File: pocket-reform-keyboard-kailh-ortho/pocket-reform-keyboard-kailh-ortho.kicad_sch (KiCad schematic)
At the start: 128 parts, among them SW1 Choc, SW10 Choc, SW11 Choc, SW12 Choc, SW13 Choc, SW14 Choc, SW15 Choc, SW16 Choc, SW17 Choc, SW18 Choc, SW19 Choc, SW2 Choc, SW20 Choc, SW21 Choc, SW22 Choc, SW23 Choc, SW24 Choc, SW25 Choc, SW26 Choc, SW27 Choc, SW28 Choc, SW29 Choc, SW3 Choc, SW30 Choc, SW31 Choc, SW32 Choc, SW33 Choc, SW34 Choc, SW35 Choc, SW36 Choc, SW37 Choc, SW38 Choc, SW39 Choc, SW4 Choc, SW40 Choc, SW41 Choc, SW42 Choc, SW43 Choc, SW44 Choc, SW45 Choc, SW46 Choc, SW47 Choc, SW48 Choc, SW49 Choc, SW5 Choc, SW50 Choc, SW51 Choc, SW52 Choc, SW53 Choc, SW54 Choc, SW55 Choc, SW56 Choc, SW57 Choc, SW58 Choc, SW59 Choc, SW6 Choc, SW60 Choc, SW61 Choc, SW62 Choc, SW63 Choc, SW64 Choc, SW7 Choc, SW8 Choc, SW9 Choc

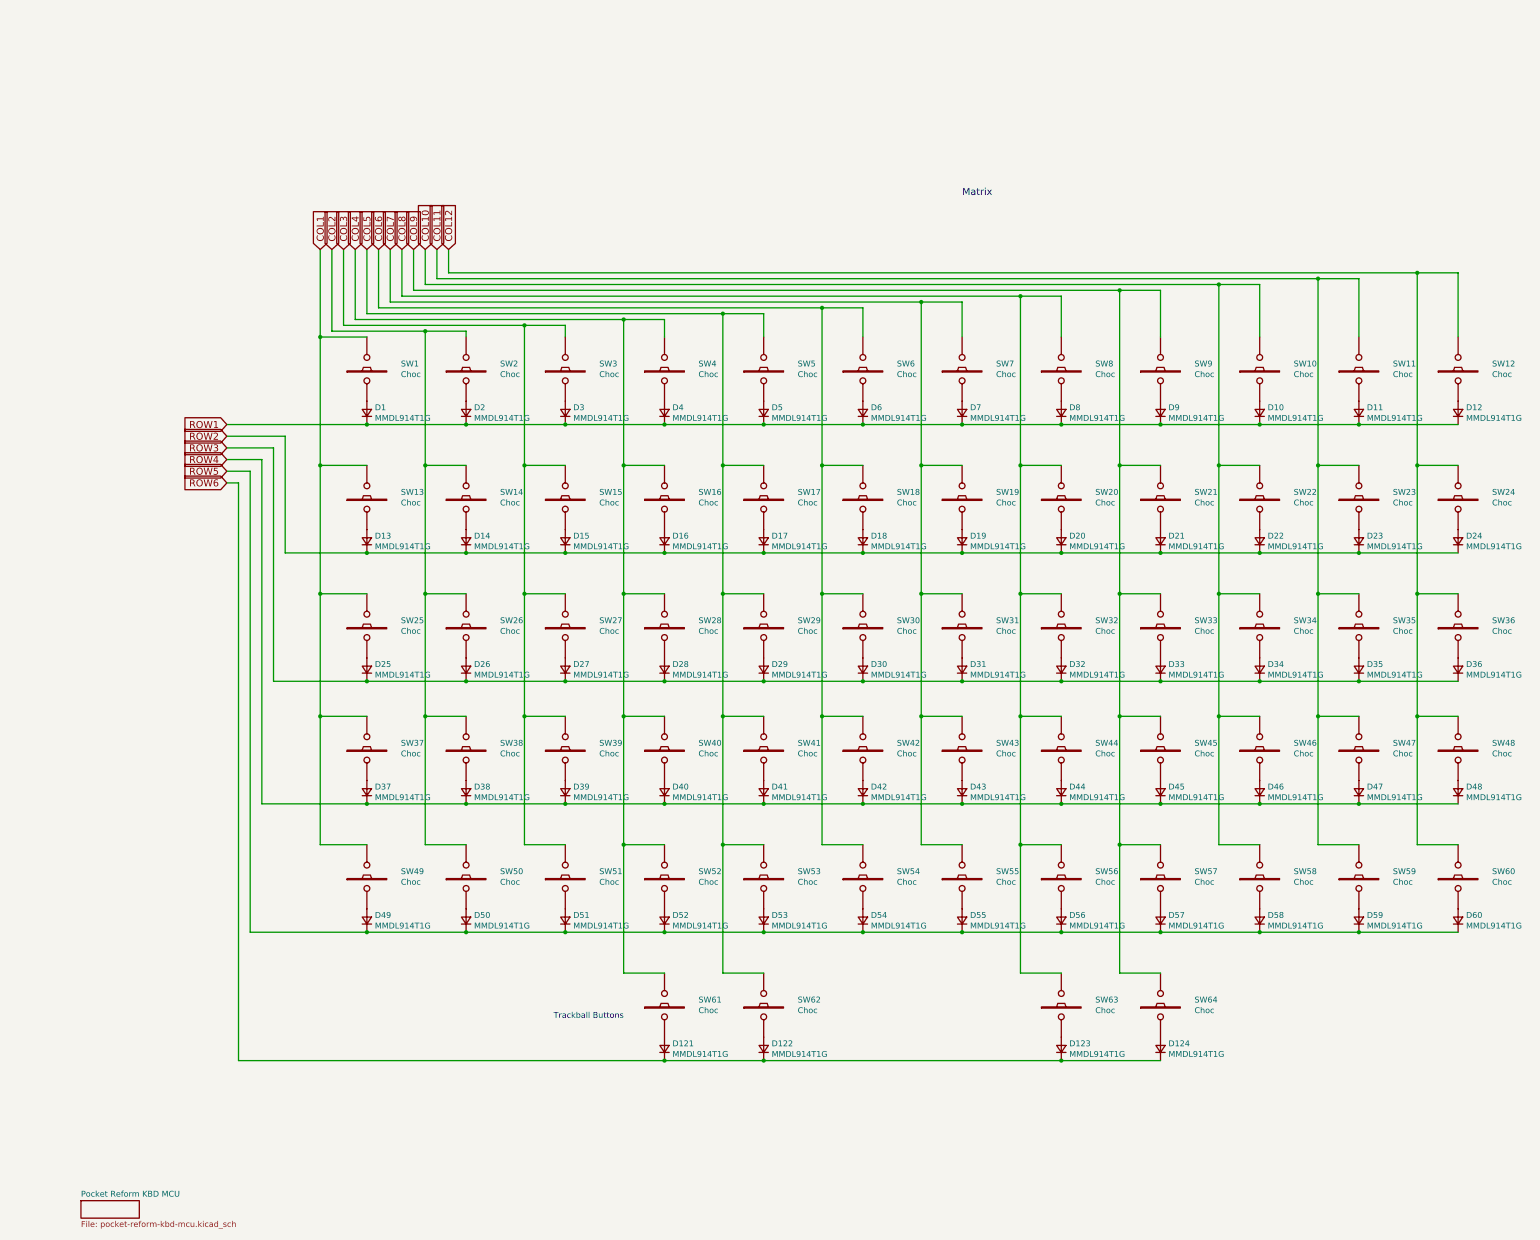
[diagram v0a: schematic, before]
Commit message: pocket keyboard 1.1 schematic and pcb mostly done
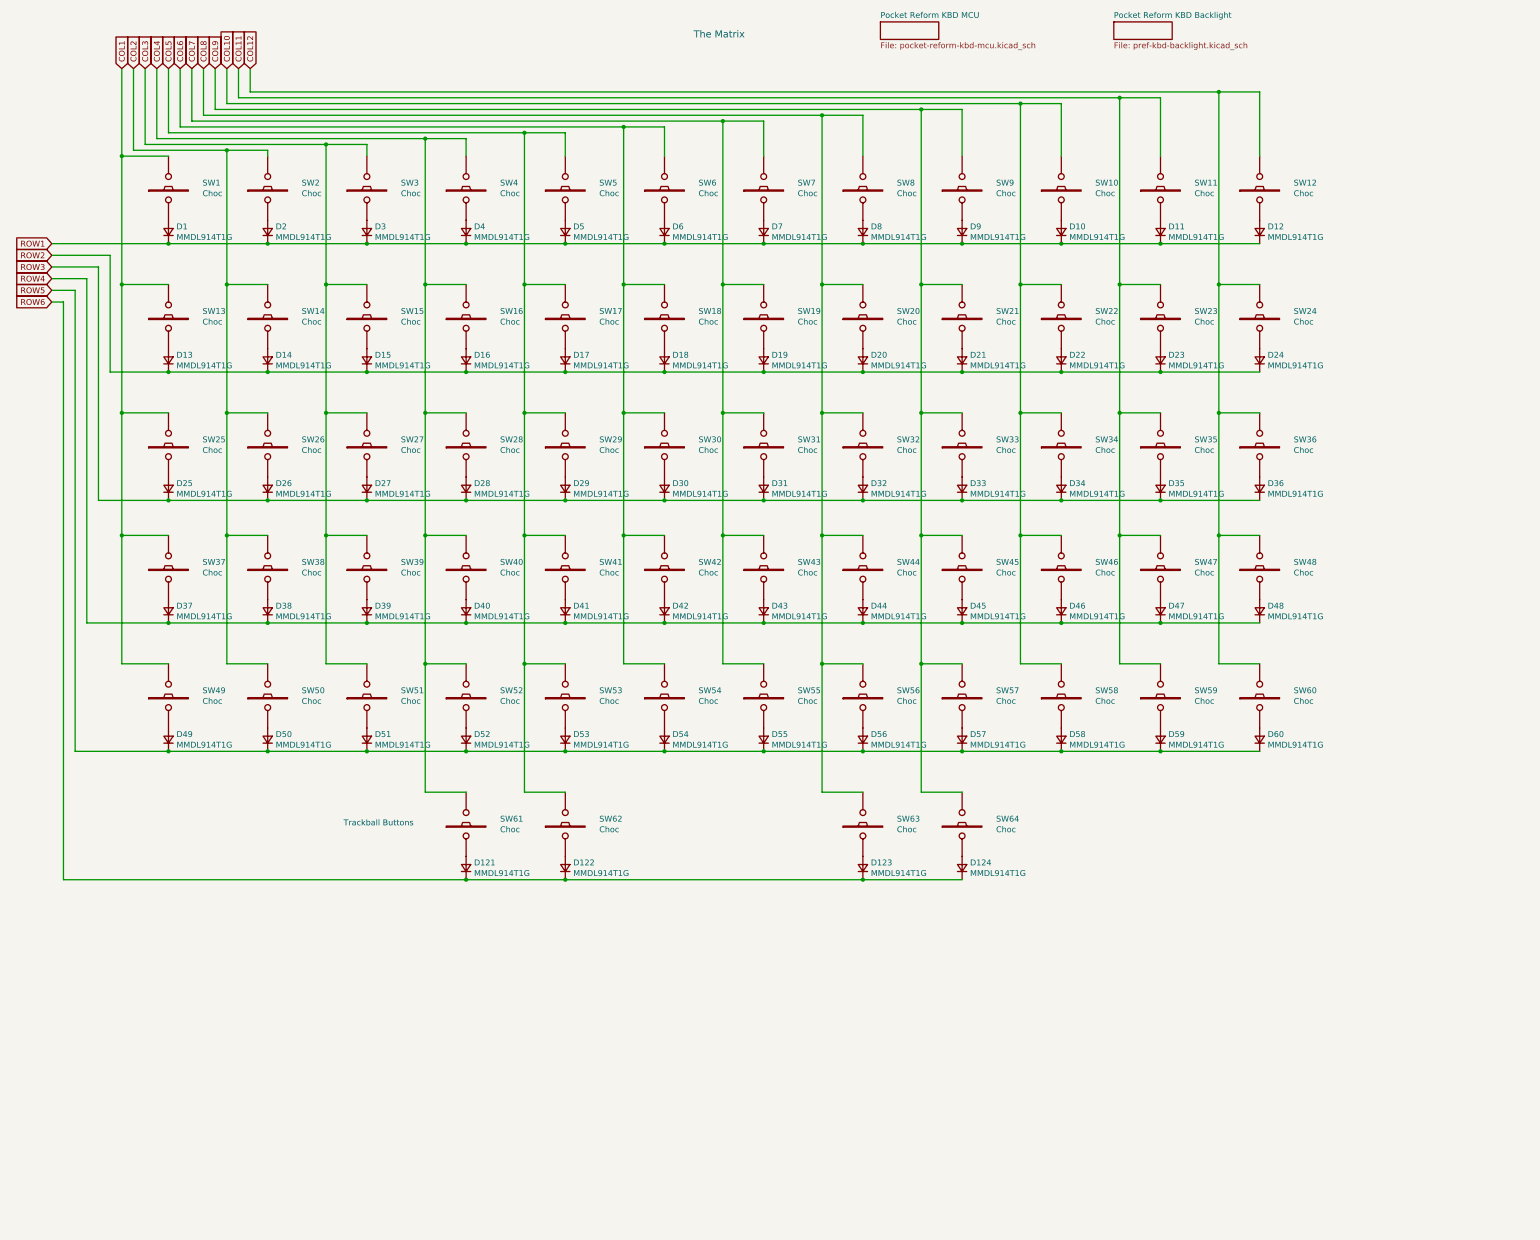
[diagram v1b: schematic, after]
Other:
- added sheet Pocket Reform KBD Backlight (pref-kbd-backlight.kicad_sch)
- note added: "The Matrix"
- note removed: "Matrix"
- moved on the sheet: D1, D10, D11, D12, D121, D122, D123, D124, D13, D14, D15, D16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

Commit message: PREF keyboard: V1.5-R1
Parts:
- D1, D10, D11, D12, D121, D122, D123, D124, D13, D14, D15, D16, D17, D18, D19, D2, D20, D21, D22, D23, D24, D25, D26, D27, D28, D29, D3, D30, D31, D32, D33, D34, D35, D36, D37, D38, D39, D4, D40, D41, D42, D43, D44, D45, D46, D47, D48, D49, D5, D50, D51, D52, D53, D54, D55, D56, D57, D58, D59, D6, D60, D7, D8, D9: LCSC C193404 -> C2128; Manufacturer ON -> Jiangsu Changjing; Manufacturer_No MMDL914T1G -> 1N4148WS
